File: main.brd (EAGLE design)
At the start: 34.3 x 54 mm, 12 parts

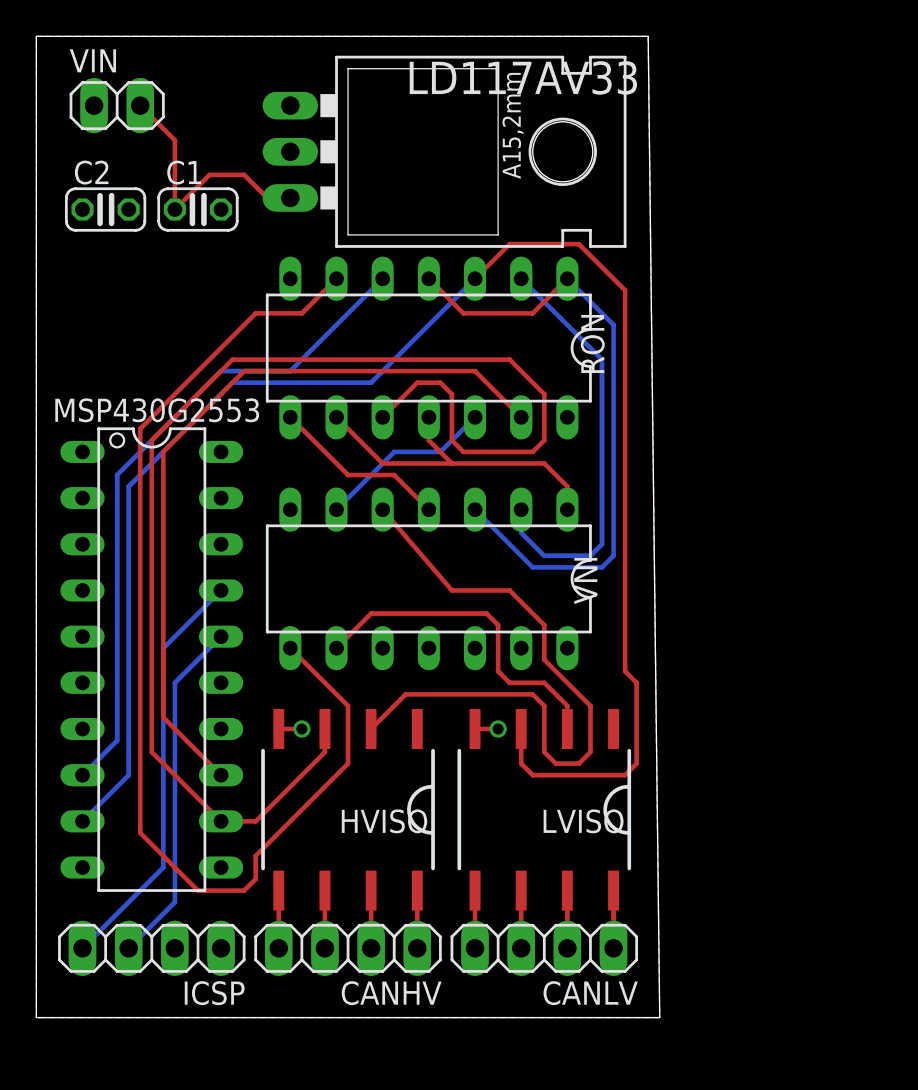
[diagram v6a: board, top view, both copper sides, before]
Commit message: Shrunk the board height a bit
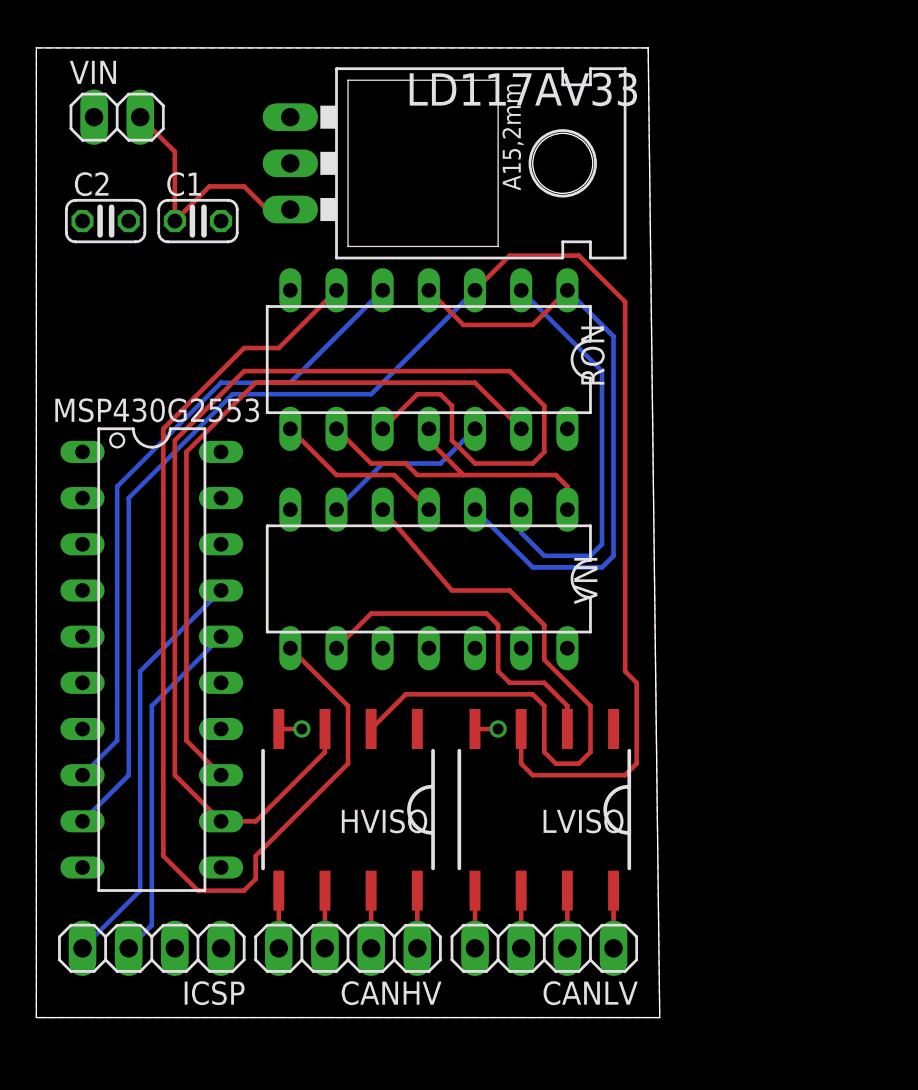
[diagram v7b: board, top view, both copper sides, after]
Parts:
- moved C1 0.64 mm to (8.89, 43.8)
- moved C2 0.64 mm to (3.81, 43.8)
- moved LD117AV33 0.63 mm to (17.8, 47.0)
- moved RON 0.63 mm to (21.6, 36.2)
- moved VIN 0.63 mm to (4.45, 49.5)
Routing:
- net N$25: track 70.9 -> 68.4 mm
- net N$22: track 41.7 -> 39.6 mm
- net N$3: track 60.5 -> 58.4 mm
- net N$24: track 88.4 -> 87.2 mm
- net N$8: track 34.7 -> 34.1 mm
- net N$4: track 23.0 -> 22.3 mm
- net N$21: track 36.4 -> 35.7 mm
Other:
- board size 34.3 x 54 mm -> 34.3 x 53.3 mm

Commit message: Rotated gates 90 CCW to achieve smaller board with much shorter traces
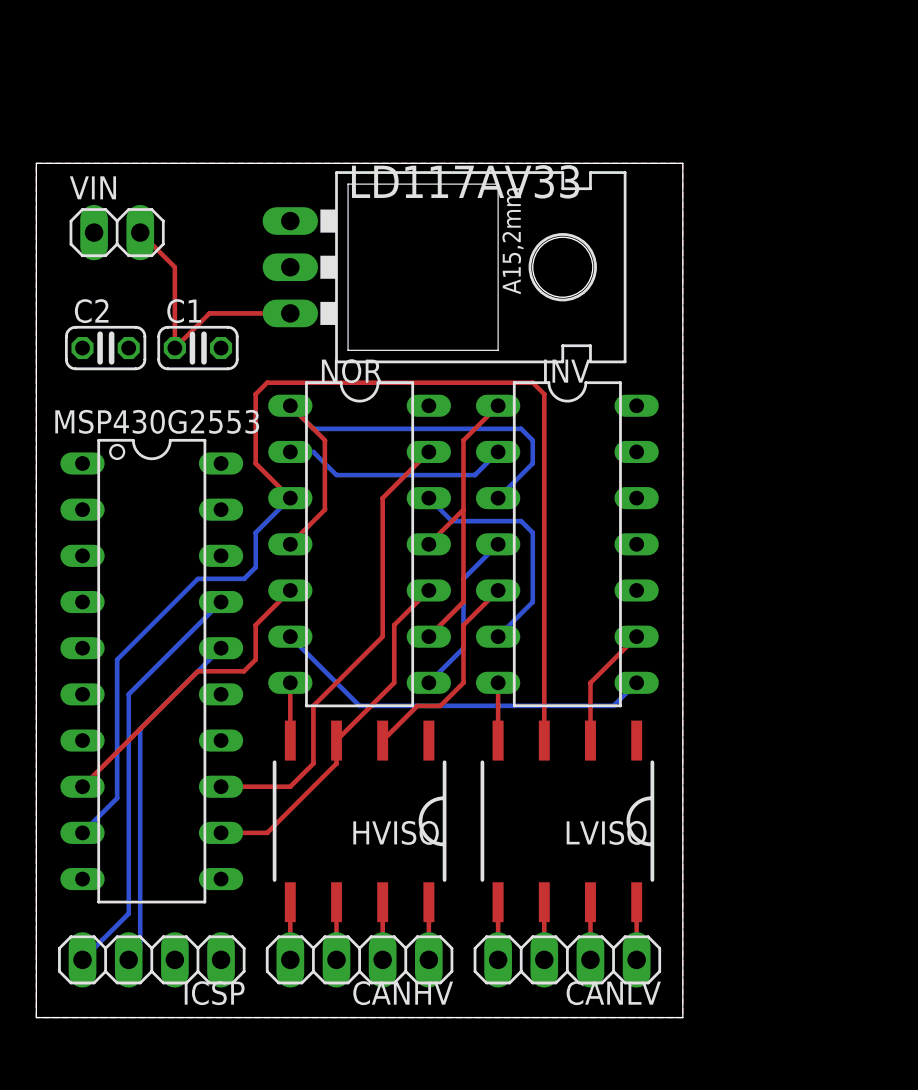
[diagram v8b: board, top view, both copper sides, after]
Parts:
- removed RON: 4001N, 40xx:DIL14
- removed VNI: 4069N, 40xx:DIL14
- added INV: 4069N, 40xx:DIL14
- added NOR: 4001N, 40xx:DIL14
- moved C1 6.98 mm to (8.89, 36.8)
- moved C2 6.98 mm to (3.81, 36.8)
- moved VIN 6.35 mm to (4.45, 43.2)
- moved LD117AV33 5.72 mm to (17.8, 41.3)
- moved CANLV 1.42 mm to (29.2, 3.17)
- moved LVISO 1.42 mm to (29.2, 10.8)
- moved CANHV 0.90 mm to (17.8, 3.17)
- moved HVISO 0.90 mm to (17.8, 10.8)
- moved ICSP 0.64 mm to (6.35, 3.17)
- moved MSP430G2553 0.63 mm to (6.35, 19.1)
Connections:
- net GND: now also INV.11, INV.13, INV.7, NOR.7; no longer RON.7, VNI.11, VNI.13, VNI.7
- net N$18: now also INV.5; no longer VNI.5
- net N$20: now also INV.9; no longer VNI.9
- net N$21: now also NOR.5; no longer RON.5
- net N$22: now also NOR.13; no longer RON.13
- net N$24: now also NOR.3; no longer RON.3
- net N$25: now also NOR.10; no longer RON.10
- net N$3: now also INV.8, NOR.6; no longer RON.6, VNI.8
- net N$4: now also INV.2, NOR.2; no longer RON.2, VNI.2
- net N$5: now also INV.4, NOR.8; no longer RON.8, VNI.4
- net N$6: now also INV.6, NOR.12; no longer RON.12, VNI.6
- net N$7: now also INV.1, NOR.11, NOR.9; no longer RON.11, RON.9, VNI.1
- net N$8: now also INV.3, NOR.1, NOR.4; no longer RON.1, RON.4, VNI.3
- net VCC: now also INV.14, NOR.14; no longer RON.14, VNI.14
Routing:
- net N$25: track 68.4 -> 19.6 mm
- net N$3: track 58.4 -> 21.2 mm
- net N$18: track 35.9 -> 11.6 mm
- net N$24: track 87.2 -> 66.6 mm
- net N$21: track 35.7 -> 17.0 mm
- net N$22: track 39.6 -> 25.4 mm
- net N$20: track 18.4 -> 6.77 mm
- net N$4: track 22.3 -> 12.5 mm
- net N$8: track 34.1 -> 27.3 mm
- net N$6: track 9.46 -> 13.0 mm
- net GND: track 3.81 -> 6.35 mm, vias 2 -> 0
- net N$7: track 18.6 -> 17.0 mm
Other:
- board size 34.3 x 53.3 mm -> 35.6 x 47 mm
